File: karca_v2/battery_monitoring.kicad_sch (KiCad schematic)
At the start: 14 parts, among them U33 INA180A2, U34 MCP3204, U35 NUP4202, U36 TLV9301xDBV

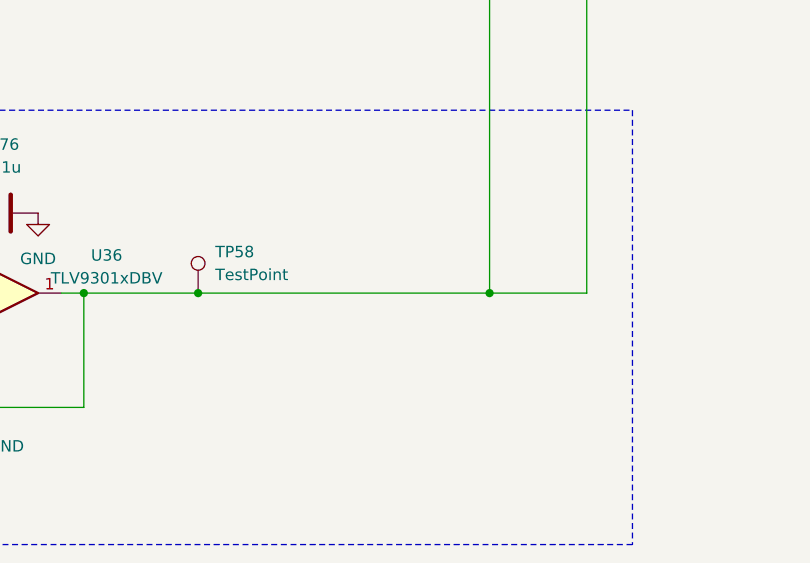
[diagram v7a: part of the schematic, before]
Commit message: Replaced header with a smaller one, added silksreen labels, and removed secondary USB power source
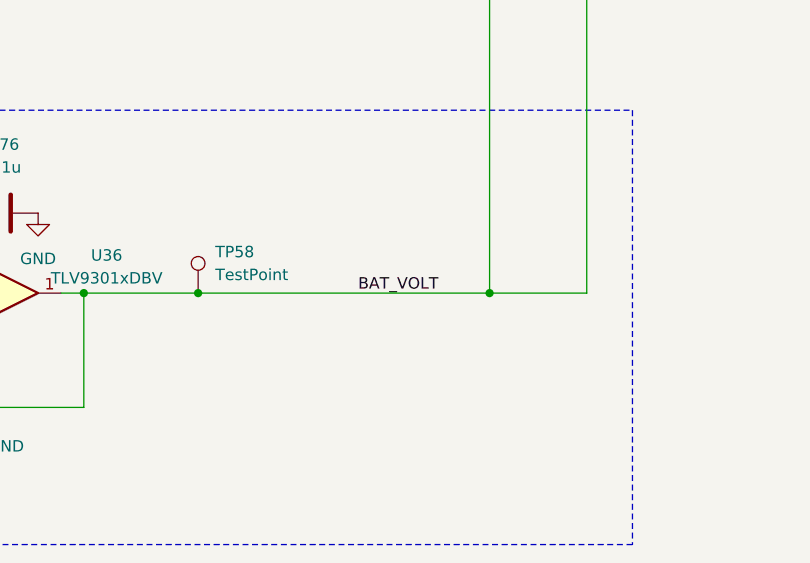
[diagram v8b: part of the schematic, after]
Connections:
- net BAT_VOLT: now reaches TP58.1, U34.2 (CH1), U35.3, U36.1, U36.4 (-)
